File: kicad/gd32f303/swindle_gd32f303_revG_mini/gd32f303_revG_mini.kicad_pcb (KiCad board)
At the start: 2 copper layers, 39.3 x 30.1 mm, 49 parts, among them J1 Debug port, J2 Debug port, J3 USB, J40 J40, J7 Conn_01x05_Pin, U1 GD32F303, U5 LM1117-3.3, Y2 8Mhz

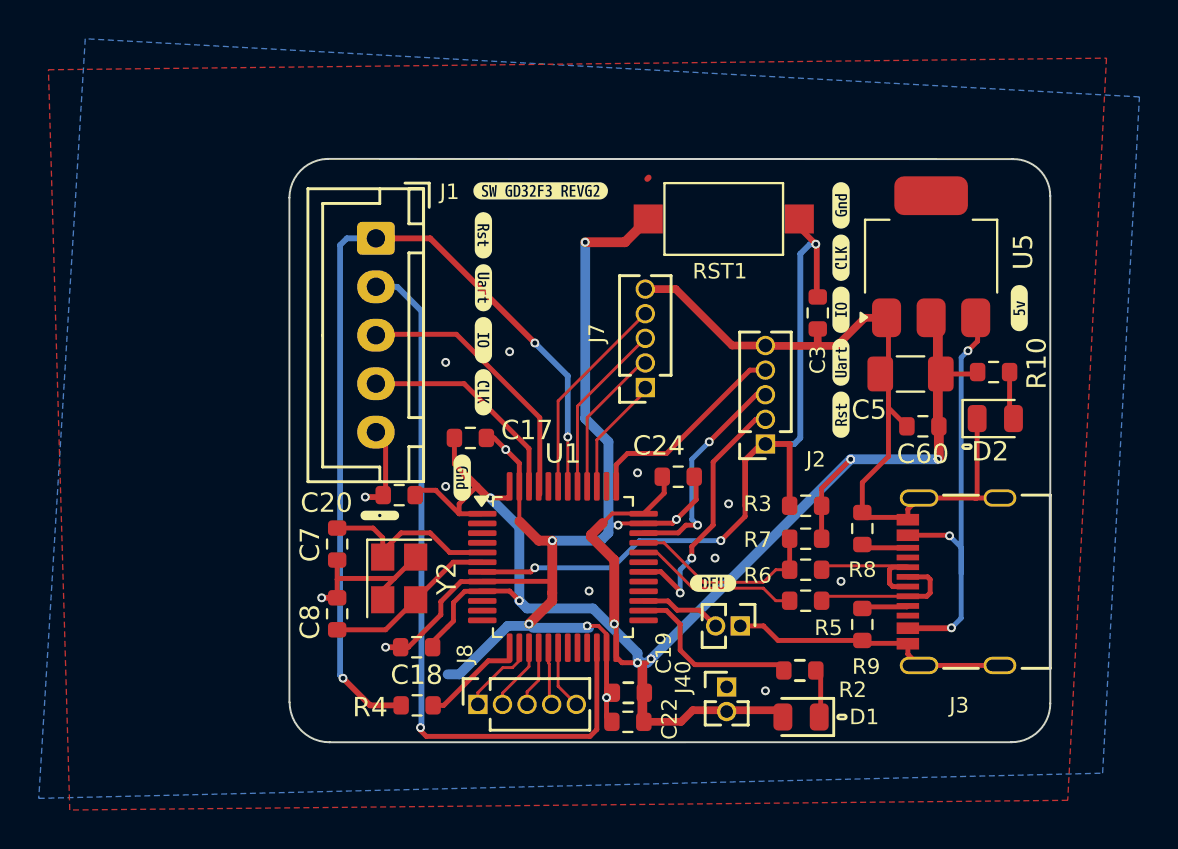
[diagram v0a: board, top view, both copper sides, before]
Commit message: add a WS2812b to the mini version, mini version for CH32,GD32 and RP2xxx
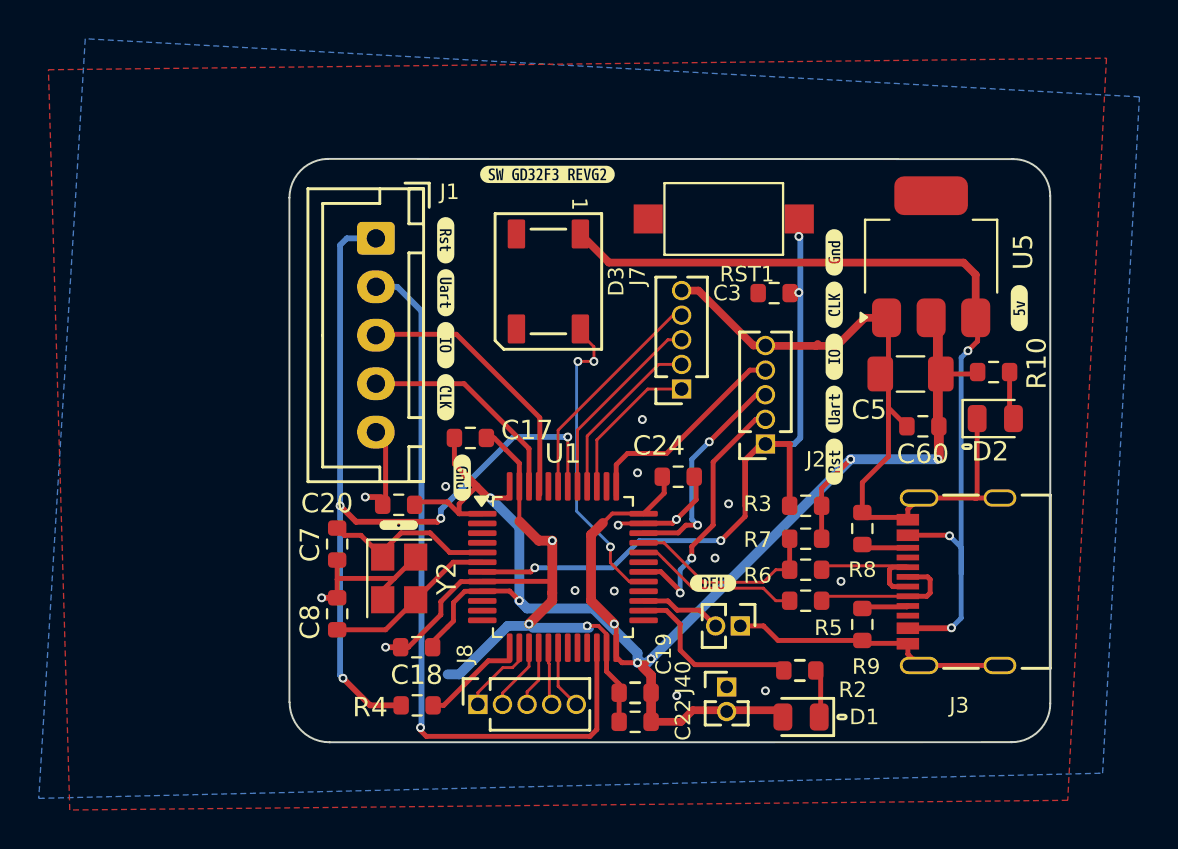
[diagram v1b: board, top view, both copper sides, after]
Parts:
- added D3: WS2812B, LED_SMD:LED_WS2812B_PLCC4_5.0x5.0mm_P3.2mm, F.Cu at (129.5, 76.2)
- moved C3 2.47 mm to (141.2, 76.8), turned to 180 degrees
- moved kibuzzard-672281E9 2.45 mm to (144.2, 85.5)
- moved kibuzzard-672281C9 2.45 mm to (144.2, 80.1)
- moved kibuzzard-672281D4 2.45 mm to (144.2, 77.4)
- moved kibuzzard-672281DC 2.45 mm to (144.2, 82.8)
- moved kibuzzard-6722820B 2.45 mm to (144.2, 74.7)
- moved kibuzzard-672281C9 1.96 mm to (124.2, 79.5)
- moved kibuzzard-672281D4 1.96 mm to (124.2, 82.2)
- moved kibuzzard-672281DC 1.96 mm to (124.2, 76.8)
- moved kibuzzard-672281E9 1.96 mm to (124.2, 74.1)
- moved J7 1.88 mm to (136.4, 81.8)
- moved kibuzzard-672226BD 1.10 mm to (121.8, 88.8)
- moved kibuzzard-68610AC9 0.92 mm to (129.4, 70.7)
- moved C20 0.50 mm to (121.8, 87.8)
- moved C22 0.38 mm to (134.0, 99.0)
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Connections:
- net Net-(U5-VI) renamed VBUS
- U1 pad 29: unconnected-(U1-PA8-Pad29) -> PA8
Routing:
- net GND: track 131.4 -> 106.1 mm, vias 20 -> 19
- net VBUS: track 23.9 -> 47.4 mm
- net PA8: track 0.00 -> 16.0 mm, vias 0 -> 3
- net NRST: track 39.4 -> 35.6 mm, vias 3 -> 4
- net PB3: track 6.41 -> 8.34 mm
- net PB4: track 8.01 -> 9.48 mm
- net PB5: track 9.56 -> 10.7 mm
- net INOUT_NRESET_3V: track 45.8 -> 44.7 mm, vias 3 -> 4
- net PB7: track 11.2 -> 12.2 mm
- net Net-(U1-PD0): track 9.51 -> 8.92 mm

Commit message: kicad: order to pcbway
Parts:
- added C1: 100n, Resistor_SMD:R_0603_1608Metric, F.Cu at (144.6, 71.5)
- added Q1: DMG2302U, Package_TO_SOT_SMD:SOT-23, F.Cu at (129.0, 80.1)
- added R1: 1k, Resistor_SMD:R_0603_1608Metric, F.Cu at (132.7, 79.2)
- added R11: 330, Resistor_SMD:R_0603_1608Metric, F.Cu at (126.3, 74.6)
- moved kibuzzard-68610AC9 7.98 mm to (121.5, 70.6)
- moved D3 1.88 mm to (130.3, 74.5)
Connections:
- D3 pad 4: PA8 -> PB4
- J1 pad 1: INOUT_NRESET_3V -> INOUT_NRESET
- R4 pad 1: INOUT_NRESET_3V -> INOUT_NRESET
- U1 pad 42: INOUT_NRESET_3V -> DRIVE_RESET
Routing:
- net INOUT_NRESET_3V: track 44.7 -> 0.00 mm, vias 4 -> 0
- net INOUT_NRESET: track 0.00 -> 33.5 mm, vias 0 -> 1
- net PA8: track 16.0 -> 0.00 mm, vias 3 -> 0
- net Net-(U1-BOOT0): track 0.00 -> 8.95 mm
- net DRIVE_RESET: track 0.00 -> 8.41 mm, vias 0 -> 2
- net PB4: track 9.48 -> 15.4 mm, vias 0 -> 1
- net Net-(Q1-D): track 0.00 -> 5.44 mm
- net VBUS: track 47.4 -> 52.2 mm
- net GND: track 106.1 -> 109.3 mm, vias 19 -> 23

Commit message: kicad : g32, cosmetic
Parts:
- added kibuzzard-68AB27BD: G***, kibuzzard-68AB27BD, F.Cu at (136.4, 84.6)
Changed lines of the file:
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@@
+		)
+	)
+	(footprint "kibuzzard-68AB27BD"
+		(layer "F.Cu")
+		(at 136.425 84.625)
+		(descr "Generated with KiBuzzard")
+		(tags "kb_params=eyJBbGlnbm1lbnRDaG9pY2UiOiAiQ2VudGVyIiwgIkNhcExlZnRDaG9pY2UiOiAiKCIsICJDYXBSaWdodENob2ljZSI6ICIpIiwgIkZvbnRDb21ib0JveCI6ICJVYnVudHVNb25vLUIiLCAiSGVpZ2h0Q3RybCI6IDEuMCwgIkxheWVyQ29tYm9Cb3giOiAiRi5TaWxrUyIsICJMaW5lU3BhY2luZ0N0cmwiOiAwLjYsICJNdWx0aUxpbmVUZXh0IjogIk5SU1QiLCAiUGFkZGluZ0JvdHRvbUN0cmwiOiAxLjAsICJQYWRkaW5nTGVmdEN0cmwiOiAwLjAsICJQYWRkaW5nUmlnaHRDdHJsIjogMC4wLCAiUGFkZGluZ1RvcEN0cmwiOiAxLjAsICJXaWR0aEN0cmwiOiAyLjgsICJhZHZhbmNlZENoZWNrYm94IjogZmFsc2UsICJpbmxpbmVGb3JtYXRUZXh0Ym94IjogZmFsc2UsICJsaW5lb3ZlclN0eWxlQ2hvaWNlIjogIlNxdWFyZSIsICJsaW5lb3ZlclRoaWNrbmVzc0N0cmwiOiAxfQ==")
+		(property "Reference" "kibuzzard-68AB27BD"
+			(at 0 -3.704435 0)
+			(layer "F.SilkS")
+			(hide yes)
+			(effects
+				(font
+					(size 0.001 0.001)
+				)
+			)
+		)
+		(property "Value" "G***"
+			(at 0 3.704435 0)
+			(layer "F.SilkS")
+			(hide yes)
+			(effects
+				(font
+					(size 0.001 0.001)
+				)
+			)
+		)
+		(property "Footprint" ""
+			(at 0 0 0)
+			(layer "F.Fab")
+			(hide yes)
+			(effects
+				(font
+					(size 1.27 1.27)
+					(thickness 0.15)
+				)
+			)
+		)
+		(property "Datasheet" ""
+			(at 0 0 0)
+			(layer "F.Fab")
+			(hide yes)
+			(effects
+				(font
+					(size 1.27 1.27)
+					(thickness 0.15)
+				)
+			)
+		)
+		(property "Description" ""
+			(at 0 0 0)
+			(layer "F.Fab")
+			(hide yes)
+			(effects
+				(font
+					(size 1.27 1.27)
+					(thickness 0.15)
+				)
+			)
+		)
+		(attr board_only exclude_from_pos_files exclude_from_bom)
+		(fp_poly
+			(pts
+				(xy -0.302908 -0.184168) (xy -0.315024 -0.252827) (xy -0.351373 -0.300485) (xy -0.407512 -0.328352)
+				(xy -0.478998 -0.337641) (xy -0.506462 -0.336834) (xy -0.538772 -0.332795) (xy -0.538772 -0.03231)
+				(xy -0.495153 -0.03231) (xy -0.407512 -0.042205) (xy -0.348142 -0.07189) (xy -0.302908 -0.184168)
+			)
+			(stroke
+				(width 0)
+				(type solid)
+			)
+			(fill solid)
+			(layer "F.SilkS")
+		)
+		(fp_poly
+			(pts
+				(xy -1.558158 -0.656435) (xy -1.558293 -0.656435) (xy -1.686357 -0.643822) (xy -1.8095 -0.606467)
+				(xy -1.922989 -0.545806) (xy -2.022463 -0.46417) (xy -2.104099 -0.364696) (xy -2.16476 -0.251207)
+				(xy -2.202115 -0.128064) (xy -2.214728 0) (xy -2.202115 0.128064) (xy -2.16476 0.251207) (xy -2.104099 0.364696)
+				(xy -2.022463 0.46417) (xy -1.922989 0.545806) (xy -1.8095 0.606467) (xy -1.686357 0.643822) (xy -1.558293 0.656435)
+				(xy -1.558158 0.656435) (xy -1.058966 0.656435) (xy -1.058966 0.500808) (xy -1.105547 0.389966)
+				(xy -1.15482 0.279304) (xy -1.206785 0.168821) (xy -1.261443 0.058338) (xy -1.318794 -0.052325)
+				(xy -1.378837 -0.163166) (xy -1.378837 0.500808) (xy -1.558158 0.500808) (xy -1.558158 -0.499192)
+				(xy -1.398223 -0.499192) (xy -1.352989 -0.425081) (xy -1.307754 -0.344911) (xy -1.263126 -0.261914)
+				(xy -1.219709 -0.179321) (xy -1.178514 -0.098142) (xy -1.140549 -0.019386) (xy -1.106826 0.053312)
+				(xy -1.078352 0.116317) (xy -1.078352 -0.499192) (xy -0.899031 -0.499192) (xy -0.899031 0.500808)
+				(xy -1.058966 0.500808) (xy -1.058966 0.656435) (xy -0.034733 0.656435) (xy -0.034733 0.500808)
+				(xy -0.243134 0.500808) (xy -0.28332 0.405695) (xy -0.329564 0.314216) (xy -0.380654 0.22395) (xy -0.43538 0.132472)
+				(xy -0.538772 0.132472) (xy -0.538772 0.500808) (xy -0.73748 0.500808) (xy -0.73748 -0.484653) (xy -0.673667 -0.496769)
+				(xy -0.603393 -0.504847) (xy -0.535541 -0.508885) (xy -0.478998 -0.510501) (xy -0.397415 -0.505654)
+				(xy -0.32391 -0.491115) (xy -0.259289 -0.466478) (xy -0.204362 -0.431341) (xy -0.127625 -0.328756)
+				(xy -0.107633 -0.261107) (xy -0.100969 -0.182553) (xy -0.109855 -0.099354) (xy -0.13651 -0.024233)
+				(xy -0.183764 0.038368) (xy -0.254443 0.084006) (xy -0.196284 0.176898) (xy -0.13651 0.283522) (xy -0.080775 0.394992)
+				(xy -0.034733 0.500808) (xy -0.034733 0.656435) (xy 0.357835 0.656435) (xy 0.357835 0.521809) (xy 0.245961 0.515145)
+				(xy 0.159128 0.495153) (xy 0.047658 0.44588) (xy 0.105816 0.28433) (xy 0.210016 0.332795) (xy 0.277262 0.349758)
+				(xy 0.357835 0.355412) (xy 0.441034 0.344911) (xy 0.493538 0.315832) (xy 0.520194 0.273829) (xy 0.527464 0.226171)
+				(xy 0.509693 0.171244) (xy 0.464459 0.128433) (xy 0.403069 0.094507) (xy 0.335218 0.066236) (xy 0.241519 0.029079)
+				(xy 0.153473 -0.024233) (xy 0.088045 -0.1042) (xy 0.062197 -0.22294) (xy 0.085016 -0.348142) (xy 0.153473 -0.442649)
+				(xy 0.221953 -0.486627) (xy 0.30569 -0.513014) (xy 0.404685 -0.521809) (xy 0.490913 -0.516559) (xy 0.565428 -0.500808)
+				(xy 0.680937 -0.453958) (xy 0.622779 -0.300485) (xy 0.533118 -0.339257) (xy 0.419225 -0.355412)
+				(xy 0.331269 -0.342667) (xy 0.278496 -0.304434) (xy 0.260905 -0.240711) (xy 0.27706 -0.189822) (xy 0.318255 -0.15105)
+				(xy 0.374798 -0.121163) (xy 0.436995 -0.096931) (xy 0.534733 -0.057351) (xy 0.628433 0.000808) (xy 0.698708 0.091276)
+				(xy 0.719305 0.152464) (xy 0.726171 0.227787) (xy 0.703352 0.352383) (xy 0.634895 0.445073) (xy 0.563543 0.487704)
+				(xy 0.47119 0.513283) (xy 0.357835 0.521809) (xy 0.357835 0.656435) (xy 1.29483 0.656435) (xy 1.29483 0.500808)
+				(xy 1.094507 0.500808) (xy 1.094507 -0.33441) (xy 0.831179 -0.33441) (xy 0.831179 -0.499192) (xy 1.558158 -0.499192)
+				(xy 1.558158 -0.33441) (xy 1.29483 -0.33441) (xy 1.29483 0.500808) (xy 1.29483 0.656435) (xy 1.558158 0.656435)
+				(xy 1.558293 0.656435) (xy 1.686357 0.643822) (xy 1.8095 0.606467) (xy 1.922989 0.545806) (xy 2.022463 0.46417)
+				(xy 2.104099 0.364696) (xy 2.16476 0.251207) (xy 2.202115 0.128064) (xy 2.214728 0) (xy 2.202115 -0.128064)
+				(xy 2.16476 -0.251207) (xy 2.104099 -0.364696) (xy 2.022463 -0.46417) (xy 1.922989 -0.545806) (xy 1.8095 -0.606467)
+				(xy 1.686357 -0.643822) (xy 1.558293 -0.656435) (xy 1.558158 -0.656435) (xy -1.558158 -0.656435)
+			)
+			(stroke
+				(width 0)
+				(type solid)
+			)
+			(fill solid)
+			(layer "F.SilkS")
 		)
 	)
@@
 		(tags "resistor")
 		(property "Reference" "C24"
-			(at -1 -1.6 0)
-			(layer "F.SilkS")
-			(effects
-				(font
-					(size 1 1)
-					(thickness 0.15)
-				)
+			(at 2.925 0.175 0)
+			(layer "F.SilkS")
+			(effects
+				(font
+					(size 0.8 0.8)
+					(thickness 0.15)
+				)

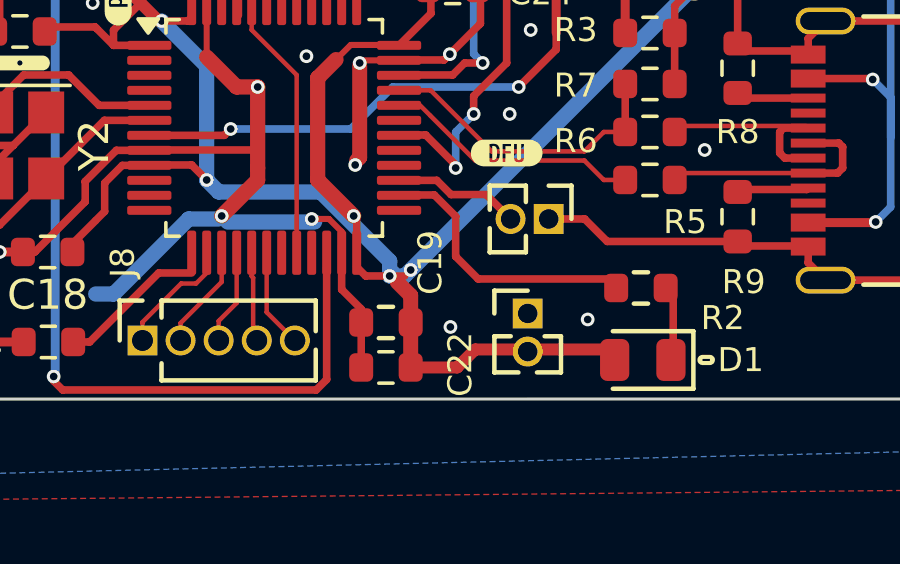
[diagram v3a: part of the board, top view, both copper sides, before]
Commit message: kicad, gd32 mini: add back the boot0 pulldown (duh)
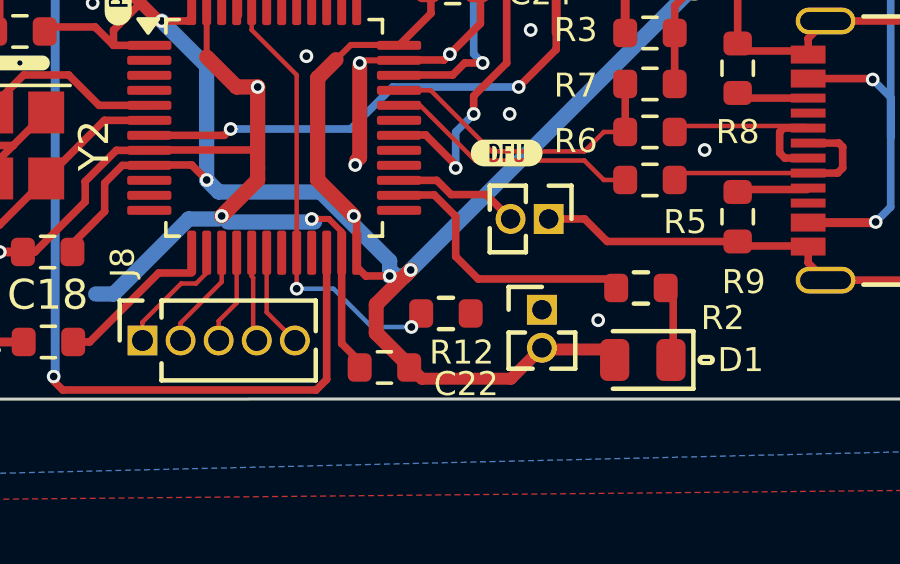
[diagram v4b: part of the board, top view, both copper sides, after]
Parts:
- removed C19: 100n, Resistor_SMD:R_0603_1608Metric
- added R12: 10k, Resistor_SMD:R_0603_1608Metric, F.Cu at (136.0, 97.2)
- moved J40 0.49 mm to (139.2, 97.0)
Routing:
- net Net-(U1-BOOT0): track 8.95 -> 14.5 mm, vias 0 -> 2
- net +3.3V: track 89.0 -> 90.4 mm
- net GND: track 109.3 -> 109.1 mm, vias 23 -> 22
